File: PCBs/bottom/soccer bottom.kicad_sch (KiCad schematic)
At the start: 52 parts, among them J1 Conn_01x04_Socket, J2 Conn_01x03_Socket, U1 CD74HC4067SM, U10 QRE1113GR, U11 QRE1113GR, U12 QRE1113GR, U13 QRE1113GR, U14 QRE1113GR, U15 QRE1113GR, U16 QRE1113GR, U17 QRE1113GR, U2 QRE1113GR, U3 QRE1113GR, U4 QRE1113GR, U5 QRE1113GR, U6 QRE1113GR, U7 QRE1113GR, U8 QRE1113GR, U9 QRE1113GR

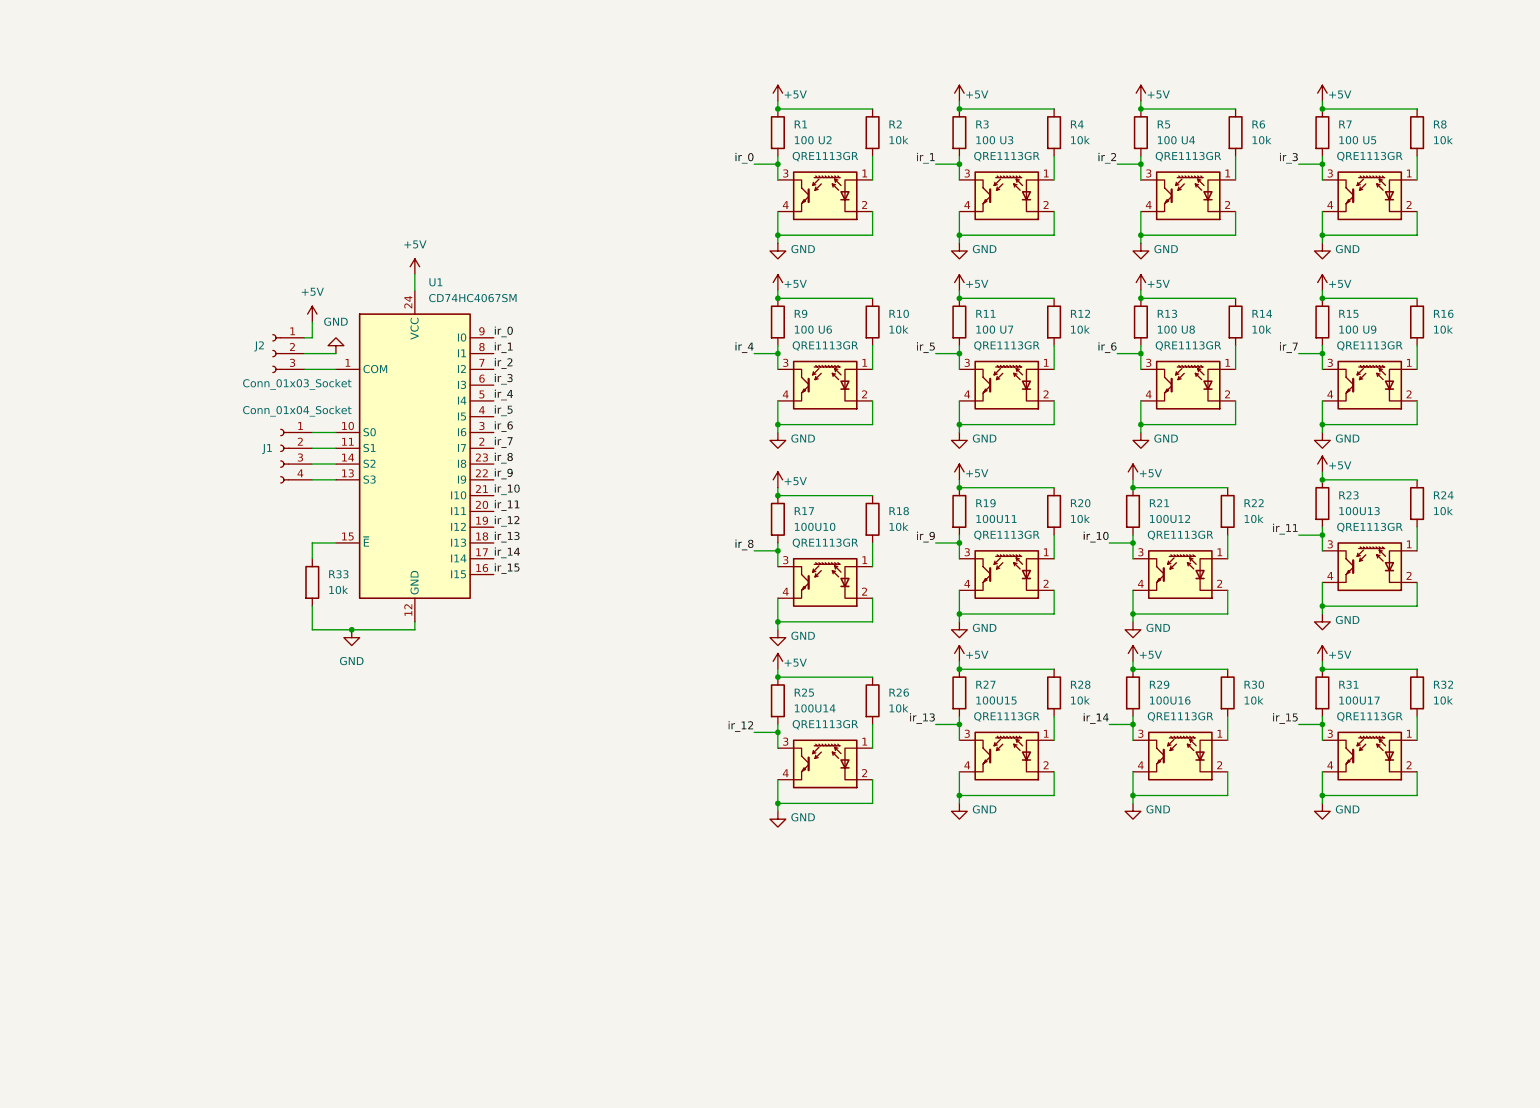
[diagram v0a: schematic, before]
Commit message: NEW MCU
rp2040-zero and mosfets

grr haven't made the pcb
schematic is good tho!
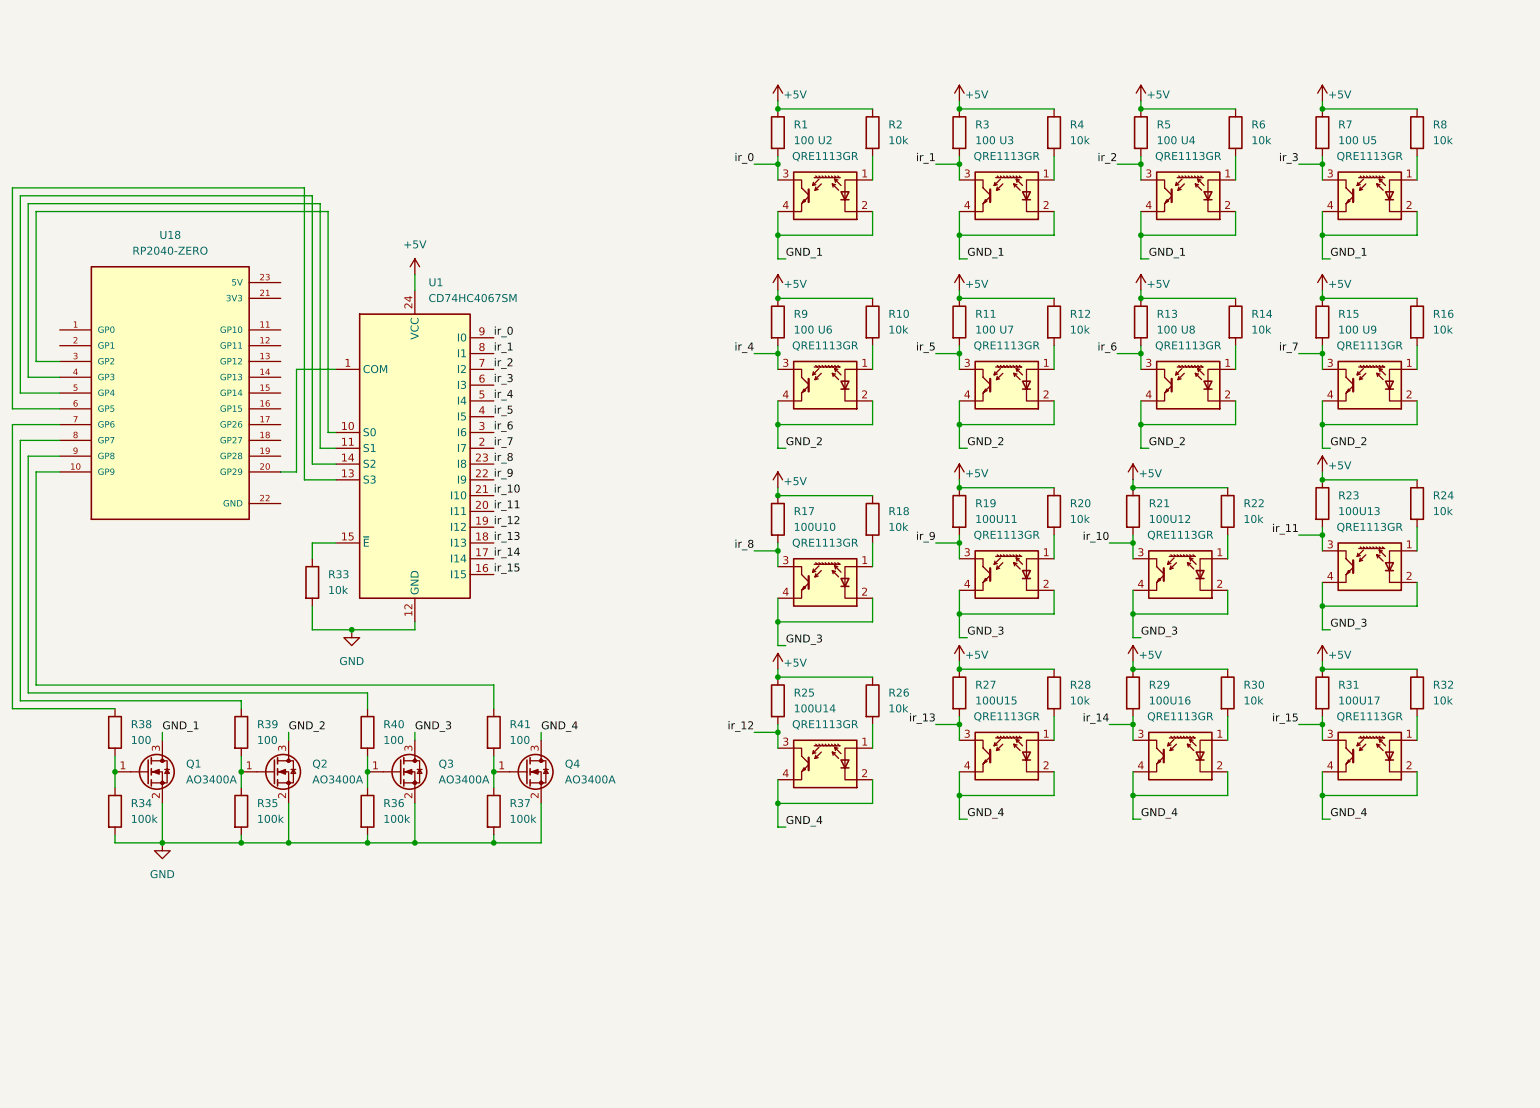
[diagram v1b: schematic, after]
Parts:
- removed J1: Conn_01x04_Socket, Connector_JST:JST_XH_B4B-XH-A_1x04_P2.50mm_Vertical, symbol Connector:Conn_01x04_Socket
- removed J2: Conn_01x03_Socket, Connector_JST:JST_XH_B3B-XH-A_1x03_P2.50mm_Vertical, symbol Connector:Conn_01x03_Socket
- added Q1, Q2, Q3, Q4: AO3400A, Package_TO_SOT_SMD:SOT-23, symbol Transistor_FET:AO3400A
- added R34, R35, R36, R37: 100k, Resistor_SMD:R_0805_2012Metric, symbol Device:R
- added R38, R39, R40, R41: 100, Resistor_SMD:R_1206_3216Metric, symbol Device:R
- added U18: RP2040-ZERO, RP2040-ZERO:MODULE_RP2040-ZERO, symbol RP2040-ZERO:RP2040-ZERO
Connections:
- net GND: now also Q1.2 (S), Q2.2 (S), Q3.2 (S), Q4.2 (S), R34.2, R35.2, R36.2, R37.2; no longer U10.2 (K), U10.4, U11.2 (K), U11.4, U12.2 (K), U12.4, U13.2 (K), U13.4, U14.2 (K), U14.4, U15.2 (K), U15.4, U16.2 (K), U16.4, U17.2 (K), U17.4, U2.2 (K), U2.4, U3.2 (K), U3.4, U4.2 (K), U4.4, U5.2 (K), U5.4, U6.2 (K), U6.4, U7.2 (K), U7.4, U8.2 (K), U8.4, U9.2 (K), U9.4
- net at U1.10 (S0): now also U18.3 (GP2)
- net at U1.11 (S1): now also U18.4 (GP3)
- net at U1.14 (S2): now also U18.5 (GP4)
- net at U1.13 (S3): now also U18.6 (GP5)
- net at U1.1 (COM): now also U18.20 (GP29)
- new net: Q1.1 (G), R34.1, R38.2
- new net: R39.1, U18.8 (GP7)
- new net: Q2.1 (G), R35.1, R39.2
- new net: R40.1, U18.9 (GP8)
- new net: Q3.1 (G), R36.1, R40.2
- new net: R41.1, U18.10 (GP9)
- new net: Q4.1 (G), R37.1, R41.2
- new net: R38.1, U18.7 (GP6)
- new net GND_1: Q1.3 (D), U2.2 (K), U2.4, U3.2 (K), U3.4, U4.2 (K), U4.4, U5.2 (K), U5.4
- new net GND_2: Q2.3 (D), U6.2 (K), U6.4, U7.2 (K), U7.4, U8.2 (K), U8.4, U9.2 (K), U9.4
- new net GND_3: Q3.3 (D), U10.2 (K), U10.4, U11.2 (K), U11.4, U12.2 (K), U12.4, U13.2 (K), U13.4
- new net GND_4: Q4.3 (D), U14.2 (K), U14.4, U15.2 (K), U15.4, U16.2 (K), U16.4, U17.2 (K), U17.4

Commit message: 100k to 10k
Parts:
- R34, R35, R36, R37: value 100k -> 10k
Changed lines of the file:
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@@
 			)
 		)
-		(property "Value" "100k"
+		(property "Value" "10k"
 			(at 86.36 147.3199 0)
 			(effects
@@
 			)
 		)
-		(property "Value" "100k"
+		(property "Value" "10k"
 			(at 106.68 147.3199 0)
 			(effects
@@
 			)
 		)
-		(property "Value" "100k"
+		(property "Value" "10k"
 			(at 45.72 147.3199 0)
 			(effects
@@
 			)
 		)
-		(property "Value" "100k"
+		(property "Value" "10k"
 			(at 66.04 147.3199 0)
 			(effects

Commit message: v2.1
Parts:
- added J1: Conn_01x04_Socket, Connector_JST:JST_XH_B4B-XH-A_1x04_P2.50mm_Vertical, symbol Connector:Conn_01x04_Socket
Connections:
- net +5V: now also U18.23 (5V), J1.3 (Pin_3)
- net GND: now also U18.22 (GND), J1.4 (Pin_4)
- net SDA: now reaches U18.13 (GP12)
- net SDA: now also J1.1 (Pin_1)
- net SCL: now reaches U18.14 (GP13)
- net SCL: now also J1.2 (Pin_2)
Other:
- moved on the sheet: Q1, Q2, Q3, Q4, R1, R10, R11, R12, R13, R14, R15, R16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

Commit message: bottom pcb update
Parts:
- added C1: 100n, Capacitor_SMD:C_0805_2012Metric, symbol Device:C
- added R42, R43: 3.3k, Resistor_SMD:R_0805_2012Metric, symbol Device:R
- J1: now not fitted; now left out of the parts list
- R1, R11, R13, R15, R17, R19, R21, R23, R25, R27, R29, R3, R31, R5, R7, R9: value 100 -> 10k; footprint Resistor_SMD:R_1206_3216Metric -> Resistor_SMD:R_0805_2012Metric
- R10, R12, R14, R16, R18, R2, R20, R22, R24, R26, R28, R30, R32, R4, R6, R8: value 10k -> 100
- R38, R39, R40, R41: footprint Resistor_SMD:R_1206_3216Metric -> Resistor_SMD:R_0805_2012Metric
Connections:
- net +5V: now also C1.1
- net GND: now also C1.2
- net SCL: now also R43.2
- net SDA: now also R42.2
- net at U18.21 (3V3): now also R42.1, R43.1
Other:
- moved on the sheet: Q1, Q2, Q3, Q4, R1, R2, R33, R34, R35, R36, R37, U1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

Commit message: bottom v2 (pcb)
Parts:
- added C2, C4: 100n, Capacitor_SMD:C_0805_2012Metric, symbol Device:C
- added C3, C5: 10u, Capacitor_SMD:C_0805_2012Metric, symbol Device:C
- added U19: AMS1117-3.3, Package_TO_SOT_SMD:SOT-223-3_TabPin2, symbol Regulator_Linear:AMS1117-3.3
- U18: footprint RP2040-ZERO:MODULE_RP2040-ZERO -> Footprints:MODULE_RP2040-ZERO; now not fitted; now left out of the parts list
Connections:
- net +5V: now also J1.4 (Pin_4), C4.1, C5.1, U19.3 (VI); no longer C1.1, J1.3 (Pin_3), R1.1, R10.1, R11.1, R12.1, R13.1, R14.1, R15.1, R16.1, R17.1, R18.1, R19.1, R2.1, R20.1, R21.1, R22.1, R23.1, R24.1, R25.1, R26.1, R27.1, R28.1, R29.1, R3.1, R30.1, R31.1, R32.1, R4.1, R5.1, R6.1, R7.1, R8.1, R9.1, U1.24 (VCC), U18.23 (5V)
- net GND: now also J1.3 (Pin_3), C2.2, C3.2, C4.2, C5.2, U19.1 (GND); no longer J1.4 (Pin_4)
- net SCL: now also J1.1 (Pin_1); no longer J1.2 (Pin_2)
- net SDA: now also J1.2 (Pin_2); no longer J1.1 (Pin_1)
- net ir_10: now also U1.18 (I13); no longer U1.21 (I10)
- net ir_11: now also U1.19 (I12); no longer U1.20 (I11)
- net ir_12: now also U1.20 (I11); no longer U1.19 (I12)
- net ir_13: now also U1.21 (I10); no longer U1.18 (I13)
- net ir_14: now also U1.22 (I9); no longer U1.17 (I14)
- net ir_15: now also U1.23 (I8); no longer U1.16 (I15)
- net ir_8: now also U1.16 (I15); no longer U1.23 (I8)
- net ir_9: now also U1.17 (I14); no longer U1.22 (I9)
- net at U1.10 (S0): now also U18.4 (GP3); no longer U18.3 (GP2)
- net at U1.11 (S1): now also U18.3 (GP2); no longer U18.4 (GP3)
- net +3.3V: now reaches R42.1, R43.1, U18.21 (3V3)
- net +3.3V: now also C1.1, R1.1, R10.1, R11.1, R12.1, R13.1, R14.1, R15.1, R16.1, R17.1, R18.1, R19.1, R2.1, R20.1, R21.1, R22.1, R23.1, R24.1, R25.1, R26.1, R27.1, R28.1, R29.1, R3.1, R30.1, R31.1, R32.1, R4.1, R5.1, R6.1, R7.1, R8.1, R9.1, U1.24 (VCC), C2.1, C3.1, U19.2 (VO)
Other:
- note added: "5V - 3.3V LDO"
- note added: "QRE1113GR sensors x16"
- note added: "processing - RP2040-Zero, CD74HC4067"
- note added: "sensor switching mosfets"
- moved on the sheet: C1, J1, Q1, Q2, Q3, Q4, R33, R34, R35, R36, R37, R38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
